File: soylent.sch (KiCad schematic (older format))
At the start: 8 parts, among them J1 DB9_Female, J2 Conn_01x04, J3 Conn_01x04, J4 Conn_02x03_Counter_Clockwise, Q1 BC847BPN, U1 ATtiny202-SS

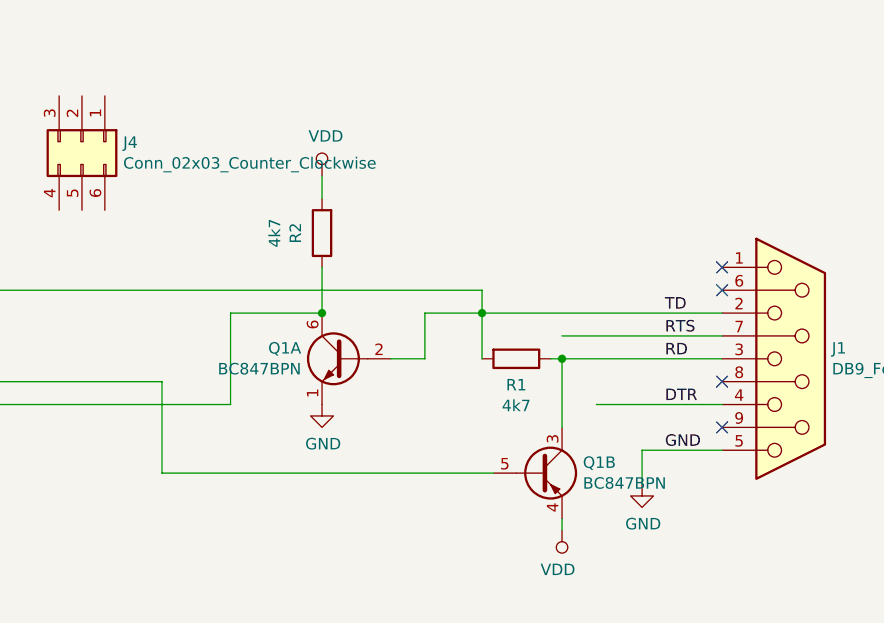
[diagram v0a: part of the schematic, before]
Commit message: Reorganize level conversion
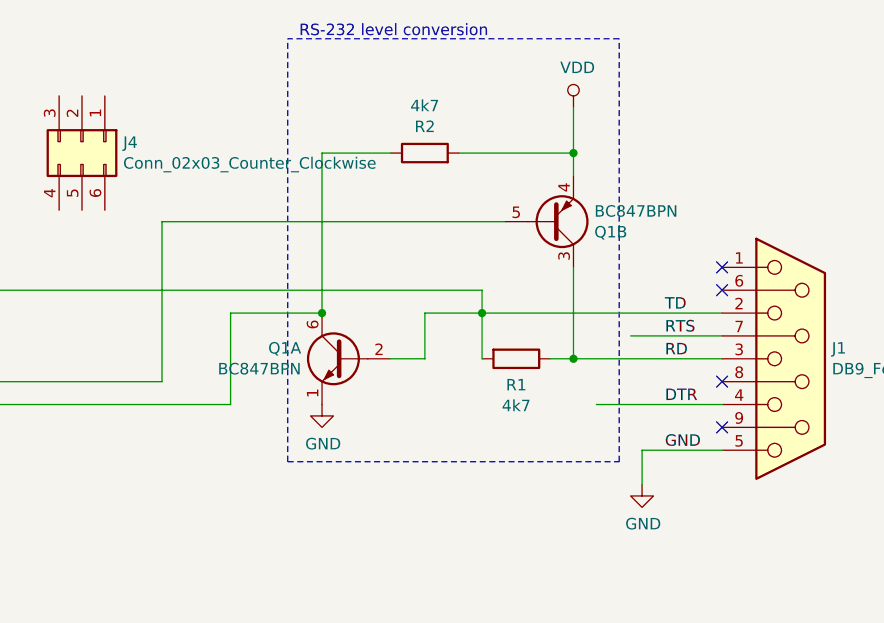
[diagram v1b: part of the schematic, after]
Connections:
- wire segments 42 -> 44
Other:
- note added: "RS-232 level conversion"
- moved on the sheet: Q1B, R2
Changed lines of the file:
@@
 	8150 4000 8700 4000
-Wire Wire Line
-	7950 3800 8000 3800
-Wire Wire Line
-	8000 3700 8700 3700
 Wire Wire Line
 	7650 3600 8700 3600
@@
 L Transistor_BJT:BC847BPN Q1
 U 2 1 5DDF77D1
-P 7900 4300
-F 0 "Q1" H 8091 4346 50  0000 L CNN
-F 1 "BC847BPN" H 8091 4255 50  0000 L CNN
-F 2 "Package_TO_SOT_SMD:SOT-363_SC-70-6" H 8100 4400 50  0001 C CNN
-F 3 "https://assets.nexperia.com/documents/data-sheet/BC847BPN.pdf" H 7900 4300 50  0001 C CNN
-	2    7900 4300
-	1    0    0    -1
+P 7950 3200
+F 0 "Q1" H 8141 3246 50  0000 L CNN
+F 1 "BC847BPN" H 8141 3155 50  0000 L CNN
+F 2 "Package_TO_SOT_SMD:SOT-363_SC-70-6" H 8150 3300 50  0001 C CNN
+F 3 "https://assets.nexperia.com/documents/data-sheet/BC847BPN.pdf" H 7950 3200 50  0001 C CNN
+	2    7950 3200
+	1    0    0    1
 $EndComp
 Wire Wire Line
@@
 L Device:R R2
 U 1 1 5DDFC6FD
-P 6950 3250
-F 0 "R2" V 7065 3250 50  0000 C CNN
-F 1 "4k7" V 7156 3250 50  0000 C CNN
-F 2 "Resistors_SMD:R_0805_HandSoldering" V 6880 3250 50  0001 C CNN
-F 3 "~" H 6950 3250 50  0001 C CNN
-	1    6950 3250
-	-1   0    0    1
-$EndComp
-Wire Wire Line
-	6950 3400 6950 3600
-$Comp
-L power:VDD #PWR0103
-U 1 1 5DDFD717
-P 6950 3000
-F 0 "#PWR0103" H 6950 2850 50  0001 C CNN
-F 1 "VDD" H 6967 3173 50  0000 C CNN
-F 2 "" H 6950 3000 50  0001 C CNN
-F 3 "" H 6950 3000 50  0001 C CNN
-	1    6950 3000
-	1    0    0    -1
-$EndComp
-Wire Wire Line
-	6950 3000 6950 3100
+P 7400 2900
+F 0 "R2" V 7515 2900 50  0000 C CNN
+F 1 "4k7" V 7606 2900 50  0000 C CNN
+F 2 "Resistors_SMD:R_0805_HandSoldering" V 7330 2900 50  0001 C CNN
+F 3 "~" H 7400 2900 50  0001 C CNN
+	1    7400 2900
+	0    -1   -1   0
+$EndComp
 $Comp
 L power:GND #PWR0104
@@
 L power:VDD #PWR0105
 U 1 1 5DDFF54C
-P 8000 4550
-F 0 "#PWR0105" H 8000 4400 50  0001 C CNN
-F 1 "VDD" H 8018 4723 50  0000 C CNN
-F 2 "" H 8000 4550 50  0001 C CNN
-F 3 "" H 8000 4550 50  0001 C CNN
-	1    8000 4550
-	-1   0    0    1
-$EndComp
-Wire Wire Line
-	8000 4550 8000 4500
-Wire Wire Line
-	8000 4100 8000 3800
-Connection ~ 8000 3800
-Wire Wire Line
-	8000 3800 8700 3800
+P 8050 2700
+F 0 "#PWR0105" H 8050 2550 50  0001 C CNN
+F 1 "VDD" H 8068 2873 50  0000 C CNN
+F 2 "" H 8050 2700 50  0001 C CNN
+F 3 "" H 8050 2700 50  0001 C CNN
+	1    8050 2700
+	1    0    0    -1
+$EndComp
 Wire Wire Line
 	4650 3900 6250 3900
-Wire Wire Line
-	6250 3900 6250 4300
-Wire Wire Line
-	6250 4300 7700 4300
 Connection ~ 4650 3900
 Wire Wire Line
@@
 	6550 3600 6950 3600
 Connection ~ 4750 4000
-Connection ~ 6950 3600
 $Comp
 L power:GND #PWR0106
@@
 Wire Wire Line
 	8350 4200 8350 4350
+Wire Wire Line
+	7950 3800 8050 3800
+Wire Wire Line
+	8300 3700 8700 3700
+Wire Wire Line
+	8050 3400 8050 3800
+Connection ~ 8050 3800
+Wire Wire Line
+	8050 3800 8700 3800
+Connection ~ 6950 3600
+Wire Wire Line
+	6250 3900 6250 3200
+Wire Wire Line
+	6250 3200 7750 3200
+Wire Wire Line
+	6950 2900 7250 2900
+Wire Wire Line
+	6950 2900 6950 3600
+Wire Wire Line
+	7550 2900 8050 2900
+Wire Wire Line
+	8050 2900 8050 2700
+Wire Wire Line
+	8050 3000 8050 2900
+Connection ~ 8050 2900
+Wire Notes Line
+	6800 4250 8250 4250
+Wire Notes Line
+	8250 4250 8250 2400
+Wire Notes Line
+	8250 2400 6800 2400
+Wire Notes Line
+	6800 4250 6800 2400
+Text Notes 6850 2400 0    50   ~ 0
+RS-232 level conversion
 $EndSCHEMATC

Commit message: Add missing base resistors
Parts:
- added R? (x2): 10k, symbol Device:R
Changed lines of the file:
@@
 	1    0    0    1
 $EndComp
-Wire Wire Line
-	7650 3600 7400 3600
-Wire Wire Line
-	7400 3600 7400 3800
-Wire Wire Line
-	7400 3800 7250 3800
 $Comp
 L Device:R R2
@@
 	6250 3900 6250 3200
 Wire Wire Line
-	6250 3200 7750 3200
-Wire Wire Line
 	6950 2900 7250 2900
 Wire Wire Line
@@
 Text Notes 6850 2400 0    50   ~ 0
 RS-232 level conversion
+$Comp
+L Device:R R?
+U 1 1 5DDEECC2
+P 7450 3200
+F 0 "R?" V 7243 3200 50  0000 C CNN
+F 1 "10k" V 7334 3200 50  0000 C CNN
+F 2 "" V 7380 3200 50  0001 C CNN
+F 3 "~" H 7450 3200 50  0001 C CNN
+	1    7450 3200
+	0    1    1    0
+$EndComp
+Wire Wire Line
+	7750 3200 7600 3200
+Wire Wire Line
+	6250 3200 7300 3200
+$Comp
+L Device:R R?
+U 1 1 5DDF3326
+P 7400 3800
+F 0 "R?" V 7193 3800 50  0000 C CNN
+F 1 "10k" V 7284 3800 50  0000 C CNN
+F 2 "" V 7330 3800 50  0001 C CNN
+F 3 "~" H 7400 3800 50  0001 C CNN
+	1    7400 3800
+	0    1    1    0
+$EndComp
+Wire Wire Line
+	7550 3800 7550 3600
+Wire Wire Line
+	7550 3600 7650 3600
 $EndSCHEMATC

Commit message: Assign footprints
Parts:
- gave numbers to parts that had none: 2
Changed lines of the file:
@@
 RS-232 level conversion
 $Comp
-L Device:R R?
+L Device:R R4
 U 1 1 5DDEECC2
 P 7450 3200
-F 0 "R?" V 7243 3200 50  0000 C CNN
+F 0 "R4" V 7243 3200 50  0000 C CNN
 F 1 "10k" V 7334 3200 50  0000 C CNN
 F 2 "" V 7380 3200 50  0001 C CNN
@@
 	6250 3200 7300 3200
 $Comp
-L Device:R R?
+L Device:R R3
 U 1 1 5DDF3326
 P 7400 3800
-F 0 "R?" V 7193 3800 50  0000 C CNN
+F 0 "R3" V 7193 3800 50  0000 C CNN
 F 1 "10k" V 7284 3800 50  0000 C CNN
 F 2 "" V 7330 3800 50  0001 C CNN

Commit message: Label breakout section
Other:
- note added: "Breakout"
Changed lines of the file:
@@
 Wire Wire Line
 	7550 3600 7650 3600
+Wire Notes Line
+	4400 2400 5050 2400
+Wire Notes Line
+	5050 2400 5050 4850
+Wire Notes Line
+	5050 4850 4400 4850
+Wire Notes Line
+	4400 4850 4400 2400
+Text Notes 4450 2400 0    50   ~ 0
+Breakout
 $EndSCHEMATC

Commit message: Switch to 0603 for resistors
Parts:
- Q1: footprint Package_TO_SOT_SMD:SOT-363_SC-70-6 -> TO_SOT_Packages_SMD:SOT-363_SC-70-6_Handsoldering
- R1, R2: footprint Resistors_SMD:R_0805_HandSoldering -> Resistors_SMD:R_0603_HandSoldering
- R3, R4: footprint (none) -> Resistors_SMD:R_0603_HandSoldering
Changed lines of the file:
@@
 F 0 "R1" V 7915 3800 50  0000 C CNN
 F 1 "4k7" V 8006 3800 50  0000 C CNN
-F 2 "Resistors_SMD:R_0805_HandSoldering" V 7730 3800 50  0001 C CNN
+F 2 "Resistors_SMD:R_0603_HandSoldering" V 7730 3800 50  0001 C CNN
 F 3 "~" H 7800 3800 50  0001 C CNN
 	1    7800 3800
@@
 F 0 "Q1" H 8141 3246 50  0000 L CNN
 F 1 "BC847BPN" H 8141 3155 50  0000 L CNN
-F 2 "Package_TO_SOT_SMD:SOT-363_SC-70-6" H 8150 3300 50  0001 C CNN
+F 2 "TO_SOT_Packages_SMD:SOT-363_SC-70-6_Handsoldering" H 8150 3300 50  0001 C CNN
 F 3 "https://assets.nexperia.com/documents/data-sheet/BC847BPN.pdf" H 7950 3200 50  0001 C CNN
 	2    7950 3200
@@
 F 0 "R2" V 7515 2900 50  0000 C CNN
 F 1 "4k7" V 7606 2900 50  0000 C CNN
-F 2 "Resistors_SMD:R_0805_HandSoldering" V 7330 2900 50  0001 C CNN
+F 2 "Resistors_SMD:R_0603_HandSoldering" V 7330 2900 50  0001 C CNN
 F 3 "~" H 7400 2900 50  0001 C CNN
 	1    7400 2900
@@
 F 0 "R4" V 7243 3200 50  0000 C CNN
 F 1 "10k" V 7334 3200 50  0000 C CNN
-F 2 "" V 7380 3200 50  0001 C CNN
+F 2 "Resistors_SMD:R_0603_HandSoldering" V 7380 3200 50  0001 C CNN
 F 3 "~" H 7450 3200 50  0001 C CNN
 	1    7450 3200
@@
 F 0 "R3" V 7193 3800 50  0000 C CNN
 F 1 "10k" V 7284 3800 50  0000 C CNN
-F 2 "" V 7330 3800 50  0001 C CNN
+F 2 "Resistors_SMD:R_0603_HandSoldering" V 7330 3800 50  0001 C CNN
 F 3 "~" H 7400 3800 50  0001 C CNN
 	1    7400 3800

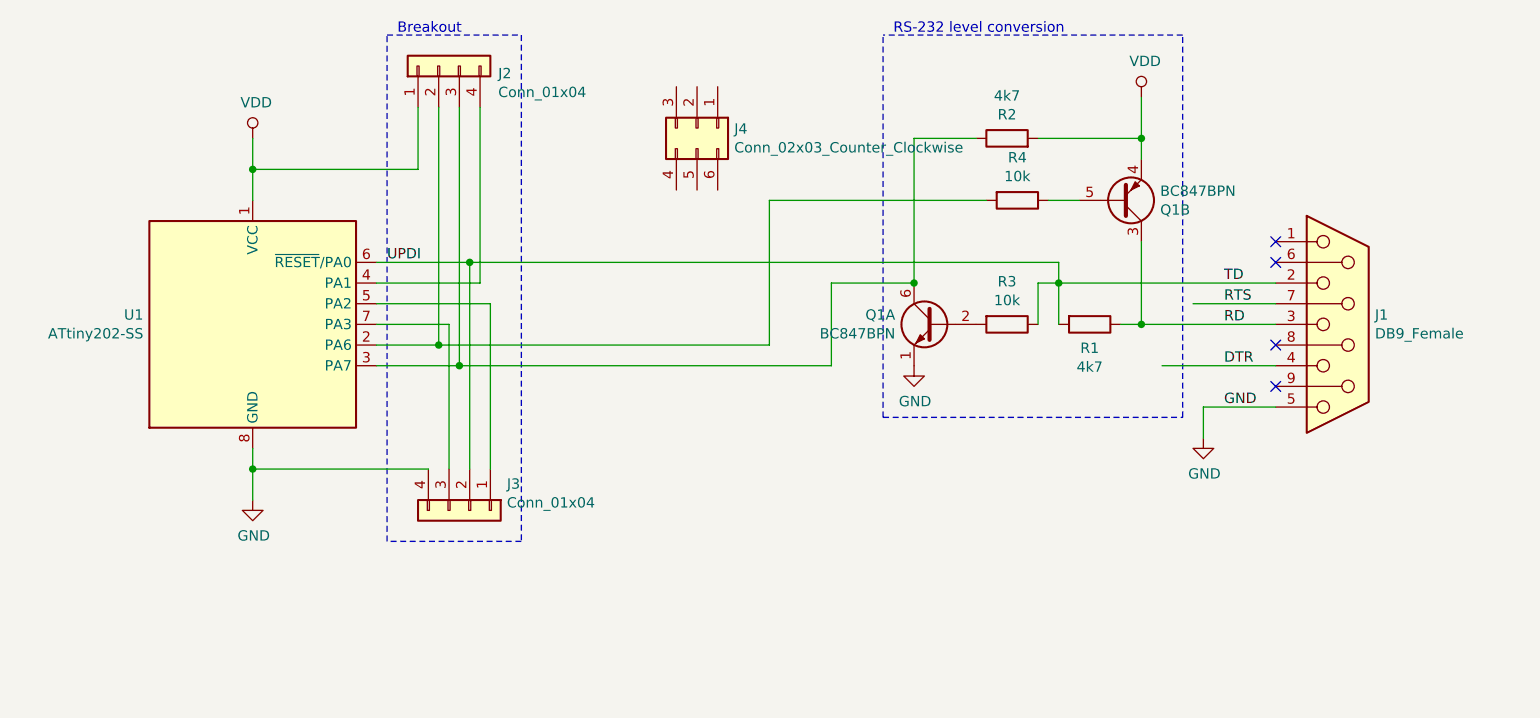
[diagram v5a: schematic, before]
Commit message: Add voltage regulator circuit
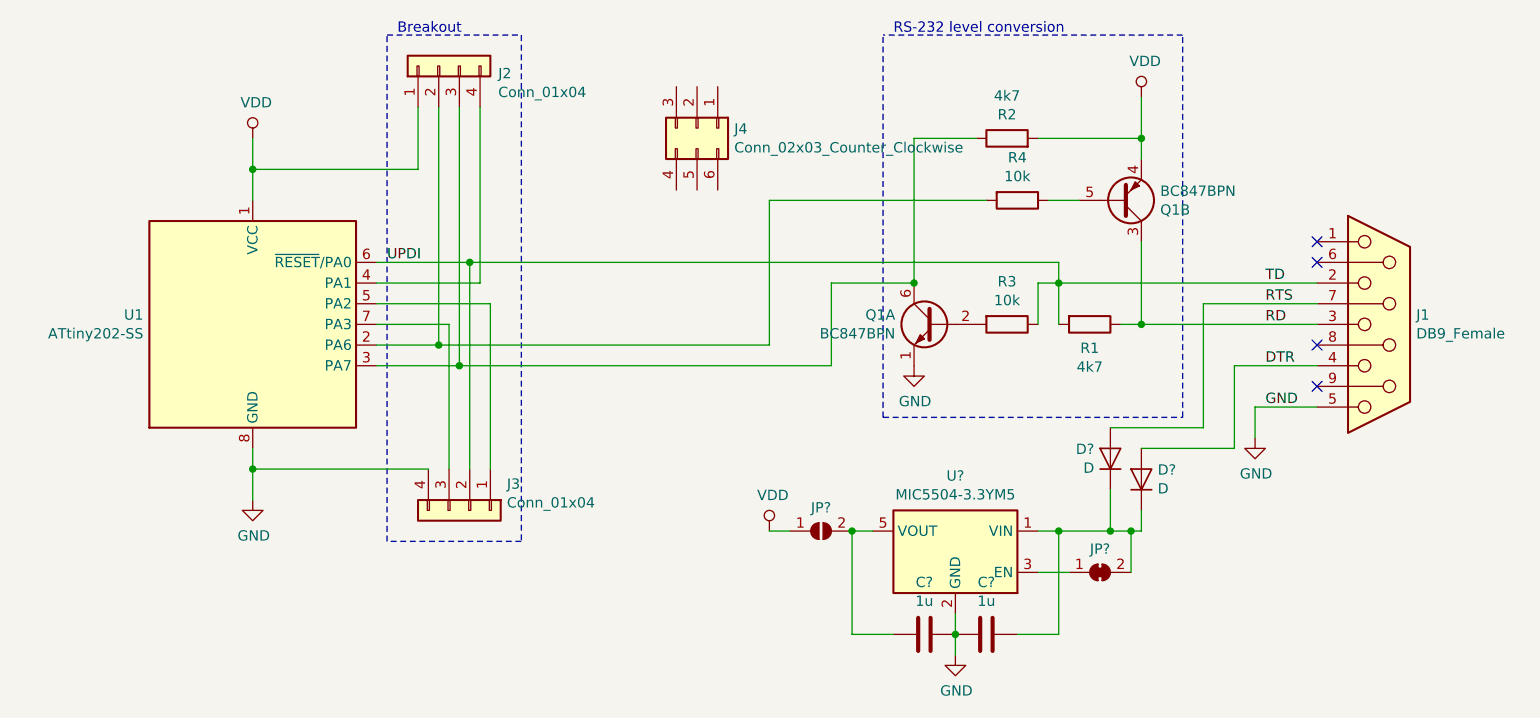
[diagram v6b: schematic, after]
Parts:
- added C? (x2): 1u, symbol Device:C
- added D? (x2): D, symbol Device:D
- added JP?: SolderJumper_2_Open, symbol Jumper:SolderJumper_2_Open
- added JP?: SolderJumper_2_Bridged, symbol Jumper:SolderJumper_2_Bridged
- added U?: MIC5504-3.3YM5, Package_TO_SOT_SMD:SOT-23-5, symbol Regulator_Linear:MIC5504-3.3YM5
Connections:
- wire segments 44 -> 64
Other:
- moved on the sheet: J1
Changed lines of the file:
@@
 L Connector:DB9_Female J1
 U 1 1 5DDD001B
-P 9000 3800
-F 0 "J1" H 9180 3846 50  0000 L CNN
-F 1 "DB9_Female" H 9180 3755 50  0000 L CNN
-F 2 "Conectors-Dsub:DSUB-9_Female_Horizontal_Pitch2.77x2.84mm_EdgePinOffset4.94mm_Housed_MountingHolesOffset7.48mm" H 9000 3800 50  0001 C CNN
-F 3 " ~" H 9000 3800 50  0001 C CNN
-	1    9000 3800
+P 9200 3800
+F 0 "J1" H 9380 3846 50  0000 L CNN
+F 1 "DB9_Female" H 9380 3755 50  0000 L CNN
+F 2 "Conectors-Dsub:DSUB-9_Female_Horizontal_Pitch2.77x2.84mm_EdgePinOffset4.94mm_Housed_MountingHolesOffset7.48mm" H 9200 3800 50  0001 C CNN
+F 3 " ~" H 9200 3800 50  0001 C CNN
+	1    9200 3800
 	1    0    0    -1
 $EndComp
@@
 	0    1    1    0
 $EndComp
-Text Label 8450 3600 0    50   ~ 0
+Text Label 8650 3600 0    50   ~ 0
 TD
-Text Label 8450 3800 0    50   ~ 0
+Text Label 8650 3800 0    50   ~ 0
 RD
-Text Label 8450 3700 0    50   ~ 0
+Text Label 8650 3700 0    50   ~ 0
 RTS
-Text Label 8450 4000 0    50   ~ 0
+Text Label 8650 4000 0    50   ~ 0
 DTR
 Wire Wire Line
 	7650 3500 7650 3600
-Wire Wire Line
-	8150 4000 8700 4000
-Wire Wire Line
-	7650 3600 8700 3600
 Connection ~ 7650 3600
 Wire Wire Line
 	7650 3600 7650 3800
-Wire Wire Line
-	8700 4200 8350 4200
-Text Label 8450 4200 0    50   ~ 0
-GND
-NoConn ~ 8700 4100
-NoConn ~ 8700 3400
-NoConn ~ 8700 3500
-NoConn ~ 8700 3900
+NoConn ~ 8900 4100
+NoConn ~ 8900 3400
+NoConn ~ 8900 3500
+NoConn ~ 8900 3900
 $Comp
 L Connector_Generic:Conn_01x04 J2
@@
 	6550 3600 6950 3600
 Connection ~ 4750 4000
-$Comp
-L power:GND #PWR0106
-U 1 1 5DE0A274
-P 8350 4350
-F 0 "#PWR0106" H 8350 4100 50  0001 C CNN
-F 1 "GND" H 8355 4177 50  0000 C CNN
-F 2 "" H 8350 4350 50  0001 C CNN
-F 3 "" H 8350 4350 50  0001 C CNN
-	1    8350 4350
-	1    0    0    -1
-$EndComp
-Wire Wire Line
-	8350 4200 8350 4350
 Wire Wire Line
 	7950 3800 8050 3800
 Wire Wire Line
-	8300 3700 8700 3700
-Wire Wire Line
 	8050 3400 8050 3800
-Connection ~ 8050 3800
-Wire Wire Line
-	8050 3800 8700 3800
 Connection ~ 6950 3600
 Wire Wire Line
@@
 Text Notes 4450 2400 0    50   ~ 0
 Breakout
+$Comp
+L power:GND #PWR0106
+U 1 1 5DE0A274
+P 8600 4350
+F 0 "#PWR0106" H 8600 4100 50  0001 C CNN
+F 1 "GND" H 8605 4177 50  0000 C CNN
+F 2 "" H 8600 4350 50  0001 C CNN
+F 3 "" H 8600 4350 50  0001 C CNN
+	1    8600 4350
+	1    0    0    -1
+$EndComp
+Text Label 8650 4200 0    50   ~ 0
+GND
+Wire Wire Line
+	8900 4200 8600 4200
+Wire Wire Line
+	8600 4200 8600 4350
+Wire Wire Line
+	7650 3600 8900 3600
+Wire Wire Line
+	8050 3800 8900 3800
+Connection ~ 8050 3800
+Wire Wire Line
+	8500 4000 8500 4400
+Wire Wire Line
+	8500 4400 8050 4400
+Wire Wire Line
+	8500 4000 8900 4000
+Wire Wire Line
+	8350 3700 8350 4300
+Wire Wire Line
+	8350 4300 7900 4300
+Wire Wire Line
+	8350 3700 8900 3700
+$Comp
+L Regulator_Linear:MIC5504-3.3YM5 U?
+U 1 1 5DE19C60
+P 7150 4900
+F 0 "U?" H 7150 5267 50  0000 C CNN
+F 1 "MIC5504-3.3YM5" H 7150 5176 50  0000 C CNN
+F 2 "Package_TO_SOT_SMD:SOT-23-5" H 7150 4500 50  0001 C CNN
+F 3 "http://ww1.microchip.com/downloads/en/DeviceDoc/MIC550X.pdf" H 6900 5150 50  0001 C CNN
+	1    7150 4900
+	-1   0    0    -1
+$EndComp
+Wire Wire Line
+	7550 5000 7700 5000
+$Comp
+L power:GND #PWR?
+U 1 1 5DE1D470
+P 7150 5400
+F 0 "#PWR?" H 7150 5150 50  0001 C CNN
+F 1 "GND" H 7155 5227 50  0000 C CNN
+F 2 "" H 7150 5400 50  0001 C CNN
+F 3 "" H 7150 5400 50  0001 C CNN
+	1    7150 5400
+	1    0    0    -1
+$EndComp
+$Comp
+L Jumper:SolderJumper_2_Open JP?
+U 1 1 5DE1E17C
+P 6500 4800
+F 0 "JP?" H 6500 4913 50  0000 C CNN
+F 1 "SolderJumper_2_Open" H 6500 4914 50  0001 C CNN
+F 2 "" H 6500 4800 50  0001 C CNN
+F 3 "~" H 6500 4800 50  0001 C CNN
+	1    6500 4800
+	1    0    0    -1
+$EndComp
+$Comp
+L power:VDD #PWR?
+U 1 1 5DE1EC76
+P 6250 4800
+F 0 "#PWR?" H 6250 4650 50  0001 C CNN
+F 1 "VDD" H 6267 4973 50  0000 C CNN
+F 2 "" H 6250 4800 50  0001 C CNN
+F 3 "" H 6250 4800 50  0001 C CNN
+	1    6250 4800
+	1    0    0    -1
+$EndComp
+$Comp
+L Jumper:SolderJumper_2_Bridged JP?
+U 1 1 5DE20E78
+P 7850 5000
+F 0 "JP?" H 7850 5113 50  0000 C CNN
+F 1 "SolderJumper_2_Bridged" H 7850 5114 50  0001 C CNN
+F 2 "" H 7850 5000 50  0001 C CNN
+F 3 "~" H 7850 5000 50  0001 C CNN
+	1    7850 5000
+	1    0    0    -1
+$EndComp
+Wire Wire Line
+	8000 5000 8000 4800
+Wire Wire Line
+	7550 4800 7650 4800
+Wire Wire Line
+	7150 5200 7150 5300
+$Comp
+L Device:C C?
+U 1 1 5DE23CE2
+P 7300 5300
+F 0 "C?" V 7048 5300 50  0000 C CNN
+F 1 "1u" V 7139 5300 50  0000 C CNN
+F 2 "" H 7338 5150 50  0001 C CNN
+F 3 "~" H 7300 5300 50  0001 C CNN
+	1    7300 5300
+	0    1    1    0
+$EndComp
+Connection ~ 7150 5300
+Wire Wire Line
+	7150 5300 7150 5400
+$Comp
+L Device:C C?
+U 1 1 5DE245AB
+P 7000 5300
+F 0 "C?" V 6748 5300 50  0000 C CNN
+F 1 "1u" V 6839 5300 50  0000 C CNN
+F 2 "" H 7038 5150 50  0001 C CNN
+F 3 "~" H 7000 5300 50  0001 C CNN
+	1    7000 5300
+	0    1    1    0
+$EndComp
+Wire Wire Line
+	6250 4800 6350 4800
+Wire Wire Line
+	6650 4800 6750 4800
+Connection ~ 6650 4800
+Wire Wire Line
+	6650 5300 6850 5300
+Wire Wire Line
+	6650 4800 6650 5300
+Wire Wire Line
+	7450 5300 7650 5300
+Wire Wire Line
+	7650 5300 7650 4800
+Connection ~ 7650 4800
+Wire Wire Line
+	7650 4800 7900 4800
+$Comp
+L Device:D D?
+U 1 1 5DE2B802
+P 7900 4450
+F 0 "D?" V 7946 4528 50  0000 L CNN
+F 1 "D" V 7855 4528 50  0000 L CNN
+F 2 "" H 7900 4450 50  0001 C CNN
+F 3 "~" H 7900 4450 50  0001 C CNN
+	1    7900 4450
+	0    -1   -1   0
+$EndComp
+$Comp
+L Device:D D?
+U 1 1 5DE2CA20
+P 8050 4550
+F 0 "D?" V 8096 4471 50  0000 R CNN
+F 1 "D" V 8005 4471 50  0000 R CNN
+F 2 "" H 8050 4550 50  0001 C CNN
+F 3 "~" H 8050 4550 50  0001 C CNN
+	1    8050 4550
+	0    -1   -1   0
+$EndComp
+Wire Wire Line
+	8050 4700 8050 4800
+Wire Wire Line
+	8050 4800 8000 4800
+Connection ~ 8000 4800
+Wire Wire Line
+	7900 4600 7900 4800
+Connection ~ 7900 4800
+Wire Wire Line
+	7900 4800 8000 4800
 $EndSCHEMATC

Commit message: Annotate schematic
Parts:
- gave numbers to parts that had none: 7
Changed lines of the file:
@@
 	8350 3700 8900 3700
 $Comp
-L Regulator_Linear:MIC5504-3.3YM5 U?
+L Regulator_Linear:MIC5504-3.3YM5 U2
 U 1 1 5DE19C60
 P 7150 4900
-F 0 "U?" H 7150 5267 50  0000 C CNN
+F 0 "U2" H 7150 5267 50  0000 C CNN
 F 1 "MIC5504-3.3YM5" H 7150 5176 50  0000 C CNN
 F 2 "Package_TO_SOT_SMD:SOT-23-5" H 7150 4500 50  0001 C CNN
@@
 	7550 5000 7700 5000
 $Comp
-L power:GND #PWR?
+L power:GND #PWR0103
 U 1 1 5DE1D470
 P 7150 5400
-F 0 "#PWR?" H 7150 5150 50  0001 C CNN
+F 0 "#PWR0103" H 7150 5150 50  0001 C CNN
 F 1 "GND" H 7155 5227 50  0000 C CNN
 F 2 "" H 7150 5400 50  0001 C CNN
@@
 $EndComp
 $Comp
-L Jumper:SolderJumper_2_Open JP?
+L Jumper:SolderJumper_2_Open JP1
 U 1 1 5DE1E17C
 P 6500 4800
-F 0 "JP?" H 6500 4913 50  0000 C CNN
+F 0 "JP1" H 6500 4913 50  0000 C CNN
 F 1 "SolderJumper_2_Open" H 6500 4914 50  0001 C CNN
 F 2 "" H 6500 4800 50  0001 C CNN
@@
 $EndComp
 $Comp
-L power:VDD #PWR?
+L power:VDD #PWR0107
 U 1 1 5DE1EC76
 P 6250 4800
-F 0 "#PWR?" H 6250 4650 50  0001 C CNN
+F 0 "#PWR0107" H 6250 4650 50  0001 C CNN
 F 1 "VDD" H 6267 4973 50  0000 C CNN
 F 2 "" H 6250 4800 50  0001 C CNN
@@
 $EndComp
 $Comp
-L Jumper:SolderJumper_2_Bridged JP?
+L Jumper:SolderJumper_2_Bridged JP2
 U 1 1 5DE20E78
 P 7850 5000
-F 0 "JP?" H 7850 5113 50  0000 C CNN
+F 0 "JP2" H 7850 5113 50  0000 C CNN
 F 1 "SolderJumper_2_Bridged" H 7850 5114 50  0001 C CNN
 F 2 "" H 7850 5000 50  0001 C CNN
@@
 	7150 5200 7150 5300
 $Comp
-L Device:C C?
+L Device:C C2
 U 1 1 5DE23CE2
 P 7300 5300
-F 0 "C?" V 7048 5300 50  0000 C CNN
+F 0 "C2" V 7048 5300 50  0000 C CNN
 F 1 "1u" V 7139 5300 50  0000 C CNN
 F 2 "" H 7338 5150 50  0001 C CNN
@@
 	7150 5300 7150 5400
 $Comp
-L Device:C C?
+L Device:C C1
 U 1 1 5DE245AB
 P 7000 5300
-F 0 "C?" V 6748 5300 50  0000 C CNN
+F 0 "C1" V 6748 5300 50  0000 C CNN
 F 1 "1u" V 6839 5300 50  0000 C CNN
 F 2 "" H 7038 5150 50  0001 C CNN
@@
 	7650 4800 7900 4800
 $Comp
-L Device:D D?
+L Device:D D1
 U 1 1 5DE2B802
 P 7900 4450
-F 0 "D?" V 7946 4528 50  0000 L CNN
+F 0 "D1" V 7946 4528 50  0000 L CNN
 F 1 "D" V 7855 4528 50  0000 L CNN
 F 2 "" H 7900 4450 50  0001 C CNN
@@
 $EndComp
 $Comp
-L Device:D D?
+L Device:D D2
 U 1 1 5DE2CA20
 P 8050 4550
-F 0 "D?" V 8096 4471 50  0000 R CNN
+F 0 "D2" V 8096 4471 50  0000 R CNN
 F 1 "D" V 8005 4471 50  0000 R CNN
 F 2 "" H 8050 4550 50  0001 C CNN
